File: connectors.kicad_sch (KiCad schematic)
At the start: 7 parts, among them J2 BM03B-SRSS-TB, J3 USB_C_Receptacle_USB2.0_16P, U2 UDT14A05L03

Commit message: reannotation
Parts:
- renumbered C40 to C1, U2 to D1, J3 to J2, J2 to J3, R45 to R1, R46 to R2
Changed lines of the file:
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@@
   (symbol (lib_id "power:GND") (at 151.13 95.25 0) (unit 1)
     (in_bom yes) (on_board yes) (dnp no)
-    (property "Reference" "#PWR081" (at 151.13 101.6 0)
+    (property "Reference" "#PWR07" (at 151.13 101.6 0)
       (effects (font (size 1.27 1.27)) hide)
     )
@@
       (project "gkos_pebble"
         (path "/ab6fff6e-44fa-4992-ab9d-8d9a7df4367d/72f5fa2a-824a-41bd-91bc-666ab65e102b"
-          (reference "#PWR081") (unit 1)
+          (reference "#PWR07") (unit 1)
         )
       )
@@
   (symbol (lib_id "Device:R") (at 143.51 121.92 0) (unit 1)
     (in_bom yes) (on_board yes) (dnp no)
-    (property "Reference" "R46" (at 144.78 120.65 0)
+    (property "Reference" "R2" (at 144.78 120.65 0)
       (effects (font (size 1.27 1.27)) (justify left))
     )
@@
       (project "gkos_pebble"
         (path "/ab6fff6e-44fa-4992-ab9d-8d9a7df4367d/72f5fa2a-824a-41bd-91bc-666ab65e102b"
-          (reference "R46") (unit 1)
+          (reference "R2") (unit 1)
         )
       )
@@
   (symbol (lib_id "power:GND") (at 135.89 127 0) (unit 1)
     (in_bom yes) (on_board yes) (dnp no)
-    (property "Reference" "#PWR083" (at 135.89 133.35 0)
+    (property "Reference" "#PWR05" (at 135.89 133.35 0)
       (effects (font (size 1.27 1.27)) hide)
     )
@@
       (project "gkos_pebble"
         (path "/ab6fff6e-44fa-4992-ab9d-8d9a7df4367d/72f5fa2a-824a-41bd-91bc-666ab65e102b"
-          (reference "#PWR083") (unit 1)
+          (reference "#PWR05") (unit 1)
         )
       )
@@
   (symbol (lib_id "power:GND") (at 217.17 116.84 0) (unit 1)
     (in_bom yes) (on_board yes) (dnp no)
-    (property "Reference" "#PWR082" (at 217.17 123.19 0)
+    (property "Reference" "#PWR08" (at 217.17 123.19 0)
       (effects (font (size 1.27 1.27)) hide)
     )
@@
       (project "gkos_pebble"
         (path "/ab6fff6e-44fa-4992-ab9d-8d9a7df4367d/72f5fa2a-824a-41bd-91bc-666ab65e102b"
-          (reference "#PWR082") (unit 1)
+          (reference "#PWR08") (unit 1)
         )
       )
@@
   (symbol (lib_id "Connector_Generic_MountingPin:Conn_01x03_MountingPin") (at 209.55 106.68 0) (mirror y) (unit 1)
     (in_bom yes) (on_board yes) (dnp no)
-    (property "Reference" "J2" (at 207.01 105.7656 0)
+    (property "Reference" "J3" (at 207.01 105.7656 0)
       (effects (font (size 1.27 1.27)) (justify left))
     )
@@
       (project "gkos_pebble"
         (path "/ab6fff6e-44fa-4992-ab9d-8d9a7df4367d/72f5fa2a-824a-41bd-91bc-666ab65e102b"
-          (reference "J2") (unit 1)
+          (reference "J3") (unit 1)
         )
       )
@@
   (symbol (lib_id "power:GND") (at 114.3 127 0) (unit 1)
     (in_bom yes) (on_board yes) (dnp no)
-    (property "Reference" "#PWR080" (at 114.3 133.35 0)
+    (property "Reference" "#PWR04" (at 114.3 133.35 0)
       (effects (font (size 1.27 1.27)) hide)
     )
@@
       (project "gkos_pebble"
         (path "/ab6fff6e-44fa-4992-ab9d-8d9a7df4367d/72f5fa2a-824a-41bd-91bc-666ab65e102b"
-          (reference "#PWR080") (unit 1)
+          (reference "#PWR04") (unit 1)
         )
       )
@@
   (symbol (lib_id "power:GND") (at 78.74 127 0) (unit 1)
     (in_bom yes) (on_board yes) (dnp no)
-    (property "Reference" "#PWR085" (at 78.74 133.35 0)
+    (property "Reference" "#PWR03" (at 78.74 133.35 0)
       (effects (font (size 1.27 1.27)) hide)
     )
@@
       (project "gkos_pebble"
         (path "/ab6fff6e-44fa-4992-ab9d-8d9a7df4367d/72f5fa2a-824a-41bd-91bc-666ab65e102b"
-          (reference "#PWR085") (unit 1)
+          (reference "#PWR03") (unit 1)
         )
       )
@@
   (symbol (lib_id "power:GND") (at 143.51 127 0) (unit 1)
     (in_bom yes) (on_board yes) (dnp no)
-    (property "Reference" "#PWR084" (at 143.51 133.35 0)
+    (property "Reference" "#PWR06" (at 143.51 133.35 0)
       (effects (font (size 1.27 1.27)) hide)
     )
@@
       (project "gkos_pebble"
         (path "/ab6fff6e-44fa-4992-ab9d-8d9a7df4367d/72f5fa2a-824a-41bd-91bc-666ab65e102b"
-          (reference "#PWR084") (unit 1)
+          (reference "#PWR06") (unit 1)
         )
       )
@@
   (symbol (lib_id "user:UDT14A05L03") (at 118.11 115.57 90) (unit 1)
     (in_bom yes) (on_board yes) (dnp no)
-    (property "Reference" "U2" (at 111.76 111.76 90)
+    (property "Reference" "D1" (at 111.76 111.76 90)
       (effects (font (size 1.27 1.27)) (justify left))
     )
@@
       (project "gkos_pebble"
         (path "/ab6fff6e-44fa-4992-ab9d-8d9a7df4367d/72f5fa2a-824a-41bd-91bc-666ab65e102b"
-          (reference "U2") (unit 1)
+          (reference "D1") (unit 1)
         )
       )
@@
   (symbol (lib_id "Device:R") (at 135.89 121.92 0) (unit 1)
     (in_bom yes) (on_board yes) (dnp no)
-    (property "Reference" "R45" (at 137.16 120.65 0)
+    (property "Reference" "R1" (at 137.16 120.65 0)
       (effects (font (size 1.27 1.27)) (justify left))
     )
@@
       (project "gkos_pebble"
         (path "/ab6fff6e-44fa-4992-ab9d-8d9a7df4367d/72f5fa2a-824a-41bd-91bc-666ab65e102b"
-          (reference "R45") (unit 1)
+          (reference "R1") (unit 1)
         )
       )
@@
   (symbol (lib_id "Device:C") (at 151.13 91.44 0) (unit 1)
     (in_bom yes) (on_board yes) (dnp no)
-    (property "Reference" "C40" (at 153.67 90.17 0)
+    (property "Reference" "C1" (at 153.67 90.17 0)
       (effects (font (size 1.27 1.27)) (justify left))
     )
@@
       (project "gkos_pebble"
         (path "/ab6fff6e-44fa-4992-ab9d-8d9a7df4367d/72f5fa2a-824a-41bd-91bc-666ab65e102b"
-          (reference "C40") (unit 1)
+          (reference "C1") (unit 1)
         )
       )
@@
   (symbol (lib_id "Connector:USB_C_Receptacle_USB2.0_16P") (at 78.74 101.6 0) (unit 1)
     (in_bom yes) (on_board yes) (dnp no) (fields_autoplaced)
-    (property "Reference" "J3" (at 78.74 78.74 0)
+    (property "Reference" "J2" (at 78.74 78.74 0)
       (effects (font (size 1.27 1.27)))
     )
@@
       (project "gkos_pebble"
         (path "/ab6fff6e-44fa-4992-ab9d-8d9a7df4367d/72f5fa2a-824a-41bd-91bc-666ab65e102b"
-          (reference "J3") (unit 1)
-        )
-      )
+          (reference "J2") (unit 1)
+        )
+      )

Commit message: change 0603 to 0805
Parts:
- J2: footprint (none) -> footprints:2171830001
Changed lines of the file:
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@@
       (effects (font (size 1.27 1.27)))
     )
-    (property "Footprint" "" (at 82.55 101.6 0)
+    (property "Footprint" "footprints:2171830001" (at 82.55 101.6 0)
       (effects (font (size 1.27 1.27)) hide)
     )

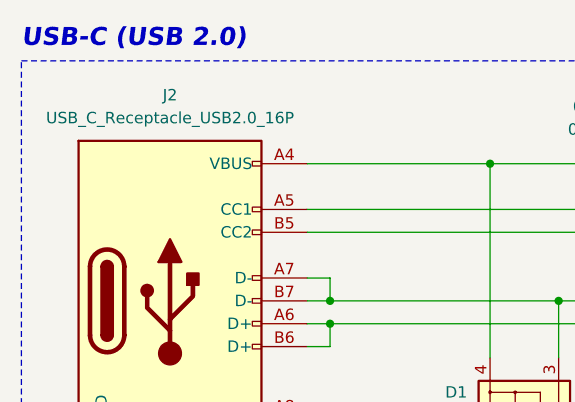
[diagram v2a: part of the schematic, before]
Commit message: add external modules
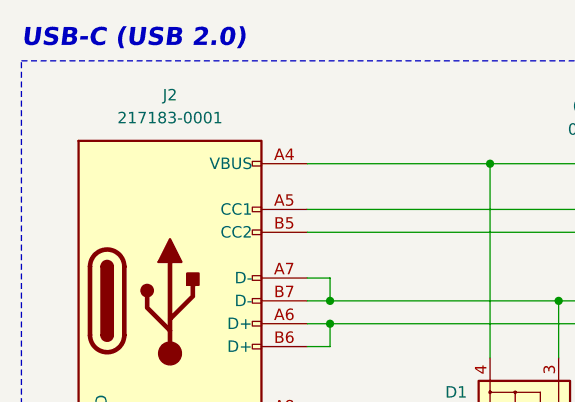
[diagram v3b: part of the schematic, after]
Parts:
- J2: value USB_C_Receptacle_USB2.0_16P -> 217183-0001
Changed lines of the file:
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@@
       (effects (font (size 1.27 1.27)))
     )
-    (property "Value" "USB_C_Receptacle_USB2.0_16P" (at 78.74 81.28 0)
+    (property "Value" "217183-0001" (at 78.74 81.28 0)
       (effects (font (size 1.27 1.27)))
     )

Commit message: schematic cleanup
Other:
- moved on the sheet: C1, D1, F1, J2, J3, R1, R2
